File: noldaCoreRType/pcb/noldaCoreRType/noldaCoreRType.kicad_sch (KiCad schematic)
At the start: 79 parts, among them J1 Conn_01x10_Female, J2 USB_C_Receptacle_USB2.0, J3 Conn_01x02_Female, J4 Conn_01x06_Female, Q1 AO3401A, SW1 SW_Push, SW10 Choc, SW11 SW_Push, SW2 Choc, SW3 Choc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

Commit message: code init (?)
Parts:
- R9: value (none) -> 10k
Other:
- note added: "THIS NEEDS TO BE FIXED!!!!"
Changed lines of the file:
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@@
+    (effects (font (size 1.27 1.27)) (justify left bottom))
+  )
+  (text "THIS NEEDS TO BE FIXED!!!!" (at 163.83 25.4 0)
     (effects (font (size 1.27 1.27)) (justify left bottom))
   )
@@
       (effects (font (size 1.27 1.27)) hide)
     )
-    (property "Value" "" (id 1) (at 48.26 68.8142 0))
+    (property "Value" "PWR_FLAG" (id 1) (at 48.26 68.8142 0))
     (property "Footprint" "" (id 2) (at 48.26 72.39 0)
       (effects (font (size 1.27 1.27)) hide)
@@
       (effects (font (size 1.27 1.27)) (justify right))
     )
-    (property "Value" "" (id 1) (at 19.05 97.79 0)
+    (property "Value" "10k" (id 1) (at 19.05 97.79 0)
       (effects (font (size 1.27 1.27)) (justify right))
     )
@@
       (effects (font (size 1.27 1.27)) hide)
     )
-    (property "Value" "" (id 1) (at 35.56 153.9042 0))
+    (property "Value" "PWR_FLAG" (id 1) (at 35.56 153.9042 0))
     (property "Footprint" "" (id 2) (at 35.56 157.48 0)
       (effects (font (size 1.27 1.27)) hide)

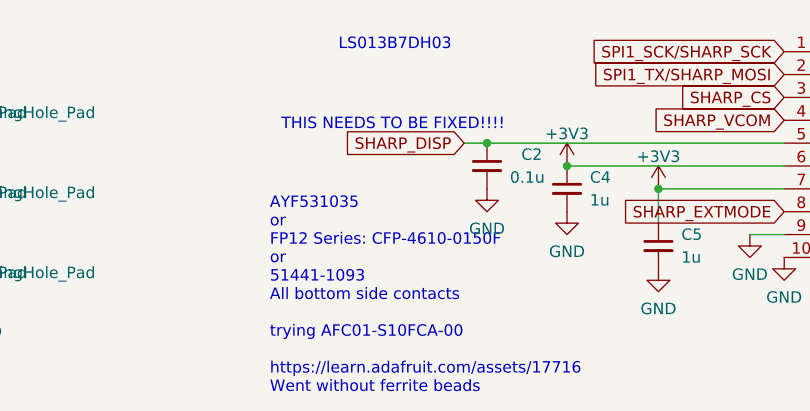
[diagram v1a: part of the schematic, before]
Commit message: add u8g2
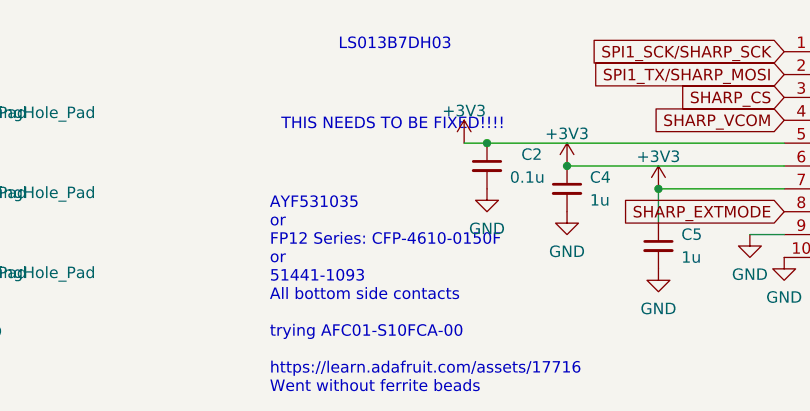
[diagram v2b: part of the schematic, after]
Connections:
- net SHARP_DISP is gone; now on net +3V3: C2.1, J1.5 (Pin_5)
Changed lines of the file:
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@@
-    )
-  )
-  (global_label "SHARP_DISP" (shape input) (at 184.15 26.67 180) (fields_autoplaced)
-    (effects (font (size 1.27 1.27)) (justify right))
-    (property "Intersheet References" "${INTERSHEET_REFS}" (id 0) (at 170.2464 26.5906 0)
-      (effects (font (size 1.27 1.27)) (justify right) hide)
     )
   )
@@
     (pin "2")
   )
+  (symbol (lib_id "power:+3V3") (at 184.15 26.67 0) (unit 1)
+    (in_bom yes) (on_board yes) (fields_autoplaced)
+    (property "Reference" "#PWR?" (id 0) (at 184.15 30.48 0)
+      (effects (font (size 1.27 1.27)) hide)
+    )
+    (property "Value" "+3V3" (id 1) (at 184.15 23.0942 0))
+    (property "Footprint" "" (id 2) (at 184.15 26.67 0)
+      (effects (font (size 1.27 1.27)) hide)
+    )
+    (property "Datasheet" "" (id 3) (at 184.15 26.67 0)
+      (effects (font (size 1.27 1.27)) hide)
+    )
+    (pin "1")
+  )
   (symbol (lib_id "Diode:BAT54C") (at 22.86 157.48 90) (unit 1)
     (in_bom yes) (on_board yes) (fields_autoplaced)
@@
       (reference "#PWR0101") (unit 1) (value "GND") (footprint "")
     )
+    (path "/bf36e9d5-29fc-4979-9020-81e493e3b1c6"
+      (reference "#PWR?") (unit 1) (value "+3V3") (footprint "")
+    )
     (path "/af385255-1fa6-45f8-bd2c-360f95357481"
